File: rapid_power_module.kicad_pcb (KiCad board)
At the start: 4 copper layers, 80 x 136 mm, 198 parts, among them J1 Conn_02x04_Top_Bottom, J11 SWD Header, J12 SWD Header, J16 USB_C_Receptacle_USB2.0, J17 TC2050, J2 Conn_02x03_Odd_Even, J3 Conn_02x04_Top_Bottom, J4 Conn_02x03_Odd_Even, J5 Molex MicroFit 2x2, J6 Molex MicroFit 2x2, J7 Molex MicroFit 2x2, J8 Molex MicroFit 2x2, J9 Molex MicroFit 2x2, Q1 Q_PMOS, Q2 Q_PMOS, Q3 Q_PMOS, Q4 Q_PMOS, Q5 NMOS, Q6 NMOS, Q7 NMOS, Q8 NMOS, SW1 KMR721NGLFS, SW2 KMR721NGLFS, U1 BQ25756RRVR, U10 L7805, U11 MCP2562-E-SN, U12 STM32F105RCTx, U13 AZ1117I-3.3, U14 TPD4E1U06, U15 TPD4E1U06, U2 CYPD3177-24LQ, U3 BQ76952PFBR, Y3 8MHz 12pF

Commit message: Further Routing work and fixed the Q Pins
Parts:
- removed Q4: Q_PMOS, Package_SO:Diodes_SO-8EP
- added Q12: AOSP21321, Package_SO:SO-8_3.9x4.9mm_P1.27mm, F.Cu at (203.9, 63.6)
- Q1, Q2, Q3: value Q_PMOS -> AOSP21321; footprint Package_SO:Diodes_SO-8EP -> Package_SO:SO-8_3.9x4.9mm_P1.27mm
- Q5, Q6, Q7, Q8: moved to F.Cu
- moved Q8 58.8 mm to (127.0, 37.2), turned to 0 degrees
- moved Q7 58.0 mm to (127.0, 43.2), turned to 0 degrees
- moved Q5 24.2 mm to (143.9, 43.3)
- moved Q6 12.6 mm to (143.9, 37.3)
- moved D24 10.8 mm to (152.5, 33.5)
- moved C12 9.68 mm to (161.8, 40.7)
- moved C13 9.68 mm to (160.8, 40.7)
- moved C9 9.68 mm to (157.1, 39.1)
- moved R18 9.68 mm to (165.8, 41.3)
- moved R5 9.68 mm to (165.6, 37.1)
- moved C10 9.68 mm to (160.5, 33.0)
- moved C11 9.68 mm to (159.7, 40.7)
- moved R10 9.68 mm to (162.7, 40.7)
- moved R13 9.68 mm to (165.5, 35.0)
- moved R19 9.68 mm to (165.7, 40.2)
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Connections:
- C10 pad 2: Net-(C10-Pad2) -> Net-(Q1-G)
- C9 pad 2: Net-(C10-Pad2) -> Net-(Q1-G)
- Q1 pad 1: (no net) -> USB_PD_OUT
- Q1 pad 2: (no net) -> USB_PD_OUT
- Q1 pad 3: (no net) -> USB_PD_OUT
- Q1 pad 4: (no net) -> Net-(Q1-G)
- Q1 pad 5: (no net) -> Net-(Q1-D-Pad5)
- Q1 pad 6: (no net) -> Net-(Q1-D-Pad5)
- Q1 pad 7: (no net) -> Net-(Q1-D-Pad5)
- Q1 pad 8: (no net) -> Net-(Q1-D-Pad5)
- Q2 pad 1: (no net) -> Net-(Q2-S-Pad1)
- Q2 pad 2: (no net) -> Net-(Q2-S-Pad1)
- Q2 pad 3: (no net) -> Net-(Q2-S-Pad1)
- Q2 pad 4: (no net) -> Net-(Q2-G)
- Q2 pad 5: (no net) -> /VBUS
- Q2 pad 6: (no net) -> /VBUS
- Q2 pad 7: (no net) -> /VBUS
- Q2 pad 8: (no net) -> /VBUS
- Q3 pad 1: (no net) -> SAFE_PWR_OUT
- Q3 pad 2: (no net) -> SAFE_PWR_OUT
- Q3 pad 3: (no net) -> SAFE_PWR_OUT
- Q3 pad 4: (no net) -> Net-(Q2-G)
- Q3 pad 5: (no net) -> Net-(Q2-S-Pad1)
- Q3 pad 6: (no net) -> Net-(Q2-S-Pad1)
- Q3 pad 7: (no net) -> Net-(Q2-S-Pad1)
- Q3 pad 8: (no net) -> Net-(Q2-S-Pad1)
- Q5 pad 4: (no net) -> unconnected-(Q5-G-Pad4)
- Q5 pad 5: (no net) -> unconnected-(Q5-D-Pad5)
- R4 pad 2: Net-(C10-Pad2) -> Net-(Q1-G)
- R5 pad 1: Net-(C10-Pad2) -> Net-(Q1-G)
- R8 pad 2: Net-(Q3-PadG) -> Net-(Q2-G)
- R9 pad 1: Net-(Q3-PadG) -> Net-(Q2-G)

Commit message: Further Routing work and fixed the Q Pins
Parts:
- removed Q8: NMOS, Package_SON:Infineon_PG-TDSON-8_6.15x5.15mm
- added Q4: HiDRV1, Package_TO_SOT_SMD:TDSON-8-1, F.Cu at (127.0, 37.0)
- added R25: 20k, Resistor_SMD:R_0402_1005Metric, F.Cu at (191.5, 46.5)
- added R27: 50k, Resistor_SMD:R_0402_1005Metric, F.Cu at (191.5, 48.5)
- Q5: value NMOS -> LoDRV1; footprint Package_SON:Infineon_PG-TDSON-8_6.15x5.15mm -> Package_TO_SOT_SMD:TDSON-8-1
- Q6: value NMOS -> HiDRV2; footprint Package_SON:Infineon_PG-TDSON-8_6.15x5.15mm -> Package_TO_SOT_SMD:TDSON-8-1
- Q7: value NMOS -> LoDRV2; footprint Package_SON:Infineon_PG-TDSON-8_6.15x5.15mm -> Package_TO_SOT_SMD:TDSON-8-1
- R83, R97: footprint Resistor_SMD:R_0603_1608Metric -> Resistor_SMD:R_0402_1005Metric
- R94: value 16k -> 20k; footprint Resistor_SMD:R_0603_1608Metric -> Resistor_SMD:R_0402_1005Metric
- R95: value 8k -> 10k; footprint Resistor_SMD:R_0603_1608Metric -> Resistor_SMD:R_0402_1005Metric
- R96: value 4k -> 5.1k; footprint Resistor_SMD:R_0603_1608Metric -> Resistor_SMD:R_0402_1005Metric
- R98: value 12.5k -> 15k
- moved C49 46.8 mm to (119.5, 42.0)
- moved Q7 17.0 mm to (144.0, 43.0), turned to 180 degrees
- moved Q5 16.9 mm to (127.0, 43.0), turned to 0 degrees
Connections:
- BT1 pad N: (no net) -> Net-(BT1--)
- BT1 pad P: (no net) -> PACK+
- BT2 pad N: (no net) -> Net-(BT2--)
- BT2 pad P: (no net) -> Net-(BT1--)
- BT3 pad N: (no net) -> PACK-
- BT3 pad P: (no net) -> Net-(BT2--)
- C1 pad 2: ISNK_FINE -> PACK-
- C11 pad 2: ISNK_FINE -> PACK-
- C12 pad 2: ISNK_FINE -> PACK-
- C13 pad 2: ISNK_FINE -> PACK-
- C16 pad 2: ISNK_FINE -> PACK-
- C17 pad 1: ISNK_FINE -> PACK-
- C19 pad 1: ISNK_FINE -> PACK-
- C2 pad 2: ISNK_FINE -> PACK-
- C21 pad 1: ISNK_FINE -> PACK-
- C24 pad 1: ISNK_FINE -> PACK-
- C3 pad 2: ISNK_FINE -> PACK-
- C37 pad 1: ISNK_FINE -> PACK-
- C38 pad 2: ISNK_FINE -> PACK-
- C4 pad 1: Net-(C4-Pad1) -> Net-(Q4-D)
- C4 pad 2: ISNK_FINE -> PACK-
- C44 pad 2: ISNK_FINE -> PACK-
- C45 pad 1: ISNK_FINE -> PACK-
- C47 pad 2: ISNK_FINE -> PACK-
- C48 pad 2: ISNK_FINE -> PACK-
- C5 pad 2: ISNK_FINE -> PACK-
- C58 pad 1: ISNK_FINE -> PACK-
- C59 pad 1: ISNK_FINE -> PACK-
- C6 pad 2: ISNK_FINE -> PACK-
- C60 pad 2: ISNK_FINE -> PACK-
- C61 pad 1: ISNK_FINE -> PACK-
- C62 pad 2: ISNK_FINE -> PACK-
- C65 pad 2: ISNK_FINE -> PACK-
- C67 pad 2: ISNK_FINE -> PACK-
- C68 pad 2: ISNK_FINE -> PACK-
- C69 pad 2: ISNK_FINE -> PACK-
- C7 pad 1: Net-(C4-Pad1) -> Net-(Q4-D)
- C7 pad 2: ISNK_FINE -> PACK-
- C70 pad 2: ISNK_FINE -> PACK-
- C71 pad 2: ISNK_FINE -> PACK-
- C72 pad 2: ISNK_FINE -> PACK-
- C73 pad 2: ISNK_FINE -> PACK-
- C74 pad 2: ISNK_FINE -> PACK-
- C75 pad 2: ISNK_FINE -> PACK-
- C76 pad 2: ISNK_FINE -> PACK-
- C77 pad 2: ISNK_FINE -> PACK-
- C78 pad 2: ISNK_FINE -> PACK-
- C79 pad 1: ISNK_FINE -> PACK-
- C8 pad 2: ISNK_FINE -> PACK-
- C80 pad 1: ISNK_FINE -> PACK-
- C81 pad 2: ISNK_FINE -> PACK-
- C82 pad 2: ISNK_FINE -> PACK-
- C83 pad 2: ISNK_FINE -> PACK-
- C84 pad 2: ISNK_FINE -> PACK-
- C85 pad 2: ISNK_FINE -> PACK-
- C86 pad 2: ISNK_FINE -> PACK-
- C87 pad 2: ISNK_FINE -> PACK-
- C88 pad 2: ISNK_FINE -> PACK-
- C89 pad 2: ISNK_FINE -> PACK-
- C90 pad 2: ISNK_FINE -> PACK-
- C91 pad 2: ISNK_FINE -> PACK-
- D20 pad 1: ISNK_FINE -> PACK-
- D21 pad 1: ISNK_FINE -> PACK-
- D24 pad 2: ISNK_FINE -> PACK-
- H1 pad 1: ISNK_FINE -> PACK-
- H2 pad 1: ISNK_FINE -> PACK-
- H3 pad 1: ISNK_FINE -> PACK-
- H4 pad 1: ISNK_FINE -> PACK-
- J1 pad 1: ISNK_FINE -> PACK-
- J1 pad 2: ISNK_FINE -> PACK-
- J11 pad 4: ISNK_FINE -> PACK-
- J12 pad 4: ISNK_FINE -> PACK-
- J16 pad A1: ISNK_FINE -> PACK-
- J16 pad A12: ISNK_FINE -> PACK-
- J16 pad B1: ISNK_FINE -> PACK-
- J16 pad B12: ISNK_FINE -> PACK-
- J16 pad S1: ISNK_FINE -> PACK-
- J17 pad 3: ISNK_FINE -> PACK-
- J17 pad 4: ISNK_FINE -> PACK-
- J2 pad 1: unconnected-(J2-Pin_1-Pad1) -> Net-(J2-Pin_1)
- J3 pad 1: ISNK_FINE -> PACK-
- J3 pad 2: ISNK_FINE -> PACK-
- J4 pad 1: unconnected-(J4-Pin_1-Pad1) -> Net-(J4-Pin_1)
- J6 pad 1: ISNK_FINE -> PACK-
- J6 pad 2: ISNK_FINE -> PACK-
- J7 pad 1: ISNK_FINE -> PACK-
- J7 pad 2: ISNK_FINE -> PACK-
- J8 pad 1: ISNK_FINE -> PACK-
- J8 pad 2: ISNK_FINE -> PACK-
- J9 pad 1: ISNK_FINE -> PACK-
- J9 pad 2: ISNK_FINE -> PACK-
- Q5 pad 1: Net-(C4-Pad1) -> PACK-
- Q5 pad 2: HIDRV1 -> PACK-
- Q5 pad 3: SW1 -> PACK-
- Q5 pad 4: unconnected-(Q5-G-Pad4) -> LODRV1
- Q5 pad 5: unconnected-(Q5-D-Pad5) -> SW1
- Q6 pad 1: SW1 -> SW2
- Q6 pad 2: LODRV1 -> SW2
- Q6 pad 3: ISNK_FINE -> SW2
- Q6 pad 4: (no net) -> HIDRV2
- Q6 pad 5: (no net) -> BuckBoostOut
- Q7 pad 1: SW2 -> PACK-
- Q7 pad 2: LODRV2 -> PACK-
- Q7 pad 3: ISNK_FINE -> PACK-
- Q7 pad 4: (no net) -> LODRV2
- Q7 pad 5: (no net) -> SW2
- R13 pad 2: ISNK_FINE -> PACK-
- R19 pad 2: ISNK_FINE -> PACK-
- R20 pad 1: ISNK_FINE -> PACK-
- R23 pad 2: ISNK_FINE -> PACK-
- R24 pad 2: ISNK_FINE -> PACK-
- R31 pad 2: ISNK_FINE -> PACK-
- R43 pad 2: ISNK_FINE -> PACK-
- R65 pad 2: Net-(C4-Pad1) -> Net-(Q4-D)
- R7 pad 2: ISNK_FINE -> PACK-
- R76 pad 1: ISNK_FINE -> PACK-
- R79 pad 1: Net-(C4-Pad1) -> Net-(Q4-D)
- R82 pad 2: ISNK_FINE -> PACK-
- R83 pad 2: ISNK_FINE -> PACK-
- R91 pad 1: ISNK_FINE -> PACK-
- R94 pad 2: ISNK_FINE -> PACK-
- R95 pad 2: ISNK_FINE -> PACK-
- R96 pad 2: ISNK_FINE -> PACK-
- R97 pad 2: ISNK_FINE -> PACK-
- R98 pad 2: ISNK_FINE -> PACK-
- SW2 pad 1: ISNK_FINE -> PACK-
- TH1 pad 2: ISNK_FINE -> PACK-
- U1 pad 17: ISNK_FINE -> PACK-
- U1 pad 22: ISNK_FINE -> PACK-
- U1 pad 37: ISNK_FINE -> PACK-
- U10 pad 2: ISNK_FINE -> PACK-
- U11 pad 2: ISNK_FINE -> PACK-
- U11 pad 8: ISNK_FINE -> PACK-
- U12 pad 12: ISNK_FINE -> PACK-
- U12 pad 18: ISNK_FINE -> PACK-
- U12 pad 31: ISNK_FINE -> PACK-
- U12 pad 47: ISNK_FINE -> PACK-
- U12 pad 63: ISNK_FINE -> PACK-
- U13 pad 1: ISNK_FINE -> PACK-
- U14 pad 3: ISNK_FINE -> PACK-
- U15 pad 3: ISNK_FINE -> PACK-
- U2 pad 19: ISNK_FINE -> PACK-
- U2 pad 22: ISNK_FINE -> PACK-
- U2 pad 25: ISNK_FINE -> PACK-
- U2 pad 6: ISNK_FINE -> PACK-
- U3 pad 17: ISNK_FINE -> PACK-
- U3 pad 18: ISNK_FINE -> PACK-
- U3 pad 20: ISNK_FINE -> PACK-
- U3 pad 41: ISNK_FINE -> PACK-
- Y3 pad 2: ISNK_FINE -> PACK-
- Y3 pad 4: ISNK_FINE -> PACK-
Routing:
- net PACK-: track 0.00 -> 16.6 mm, vias 0 -> 1
- net ISNK_FINE: track 13.3 -> 0.00 mm
- net (no net): track 145.4 -> 142.1 mm, vias 1 -> 0

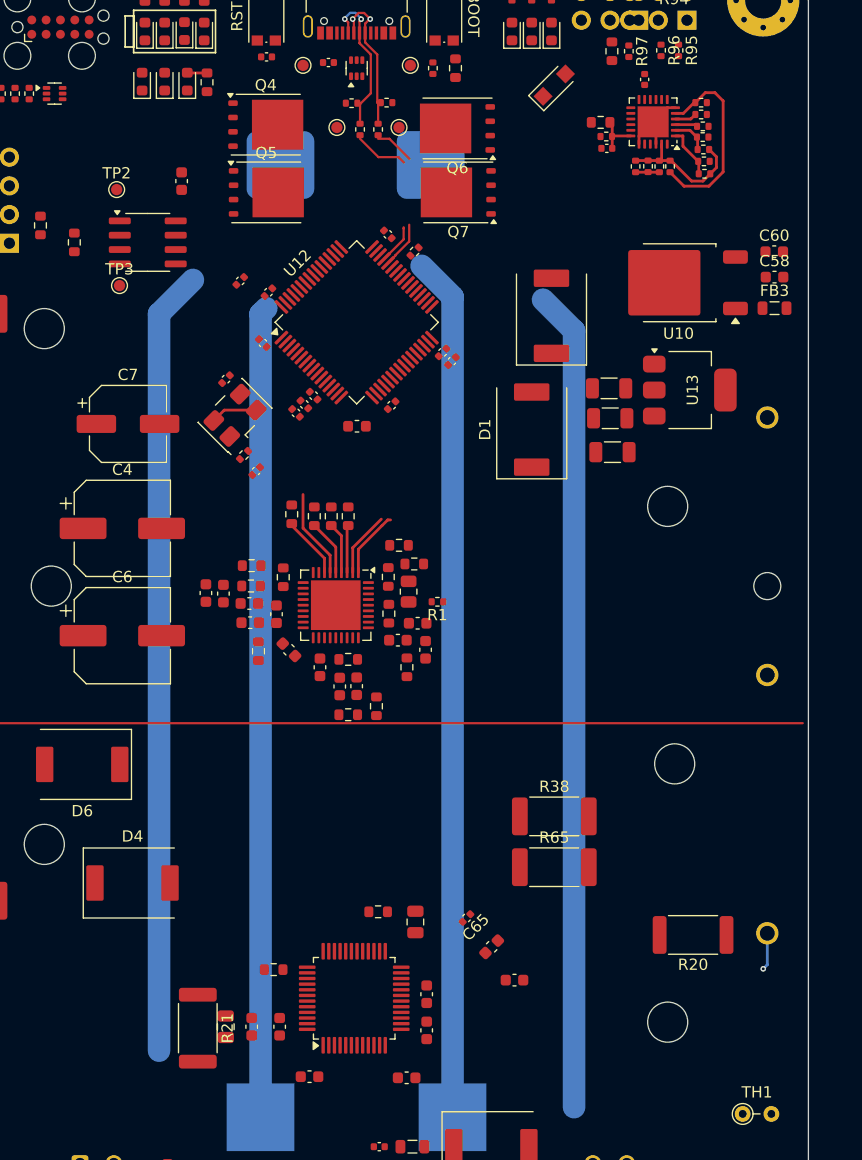
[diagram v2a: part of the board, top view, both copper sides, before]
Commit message: Placed the  NMOS near Inductor, moved STM out of the way and fixed the Battery Pins
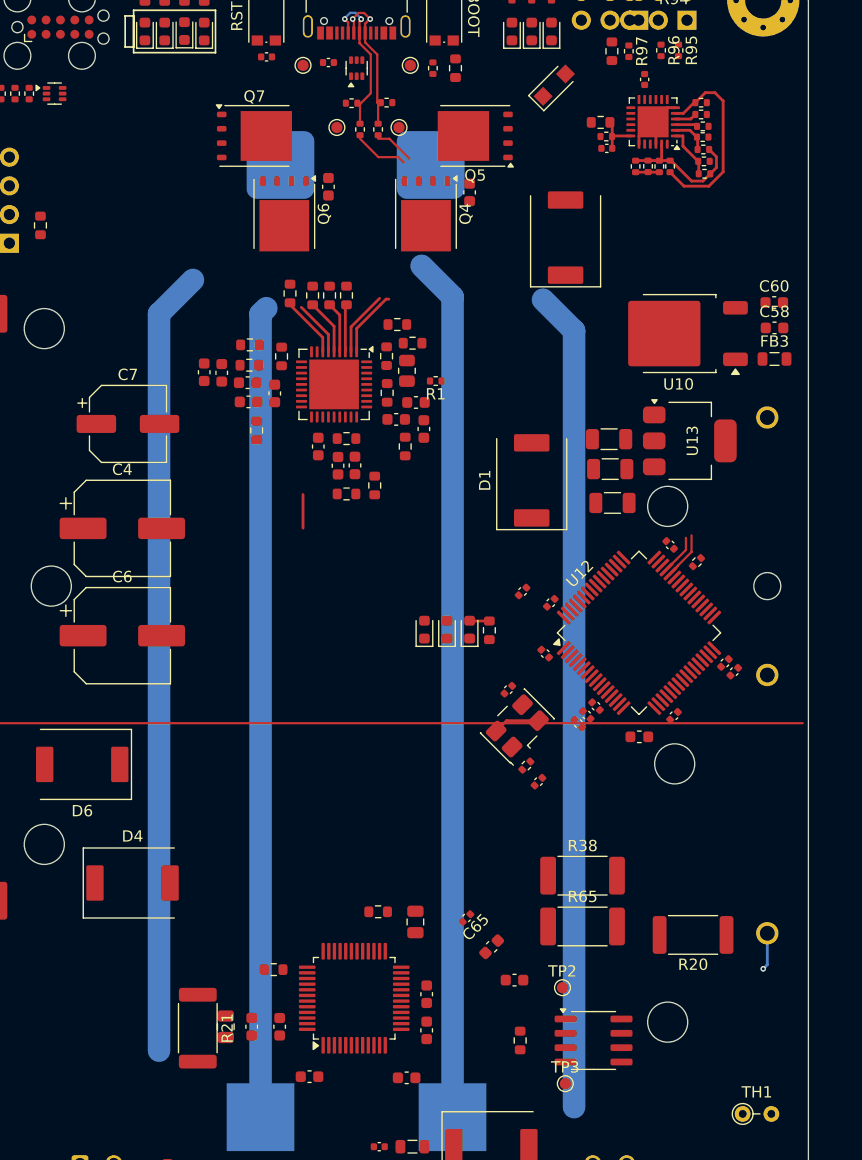
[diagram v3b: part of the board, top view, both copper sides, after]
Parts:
- moved R35 80.9 mm to (149.5, 118.1)
- moved TP2 80.9 mm to (153.2, 113.4)
- moved TP3 80.9 mm to (153.5, 121.9)
- moved U11 80.9 mm to (156.0, 118.1)
- moved D20 54.6 mm to (141.0, 81.7)
- moved D21 54.6 mm to (143.0, 81.7)
- moved D22 54.6 mm to (145.0, 81.7)
- moved R69 54.6 mm to (146.8, 81.8)
- moved C46 41.1 mm to (132.5, 42.5), turned to -90 degrees
- moved C73 37.2 mm to (156.2, 88.5)
- moved C77 37.2 mm to (151.1, 95.2)
- moved R74 37.2 mm to (150.0, 93.8)
- moved Y3 37.2 mm to (149.2, 90.2)
- moved C70 37.2 mm to (162.8, 74.2)
- moved C71 37.2 mm to (167.6, 84.7)
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
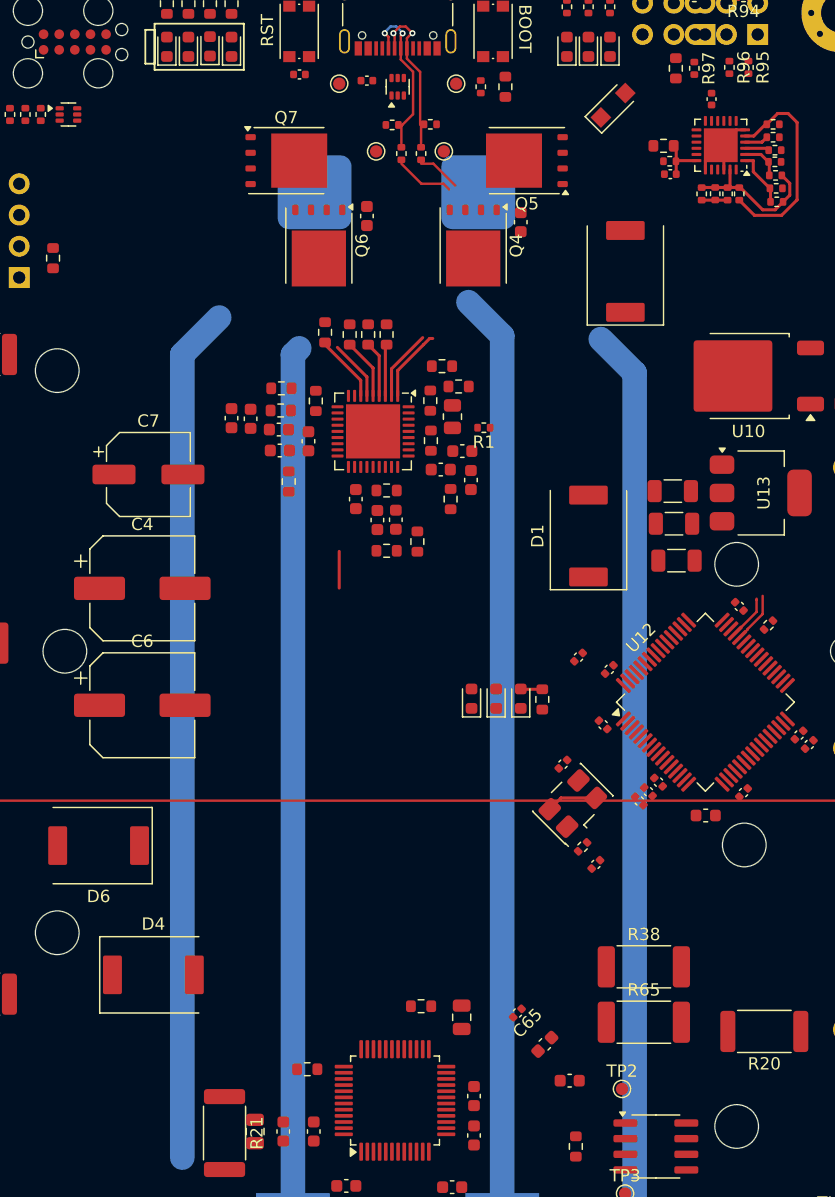
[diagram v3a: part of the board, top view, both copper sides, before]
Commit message: Fixed wuerth cap footprints and values
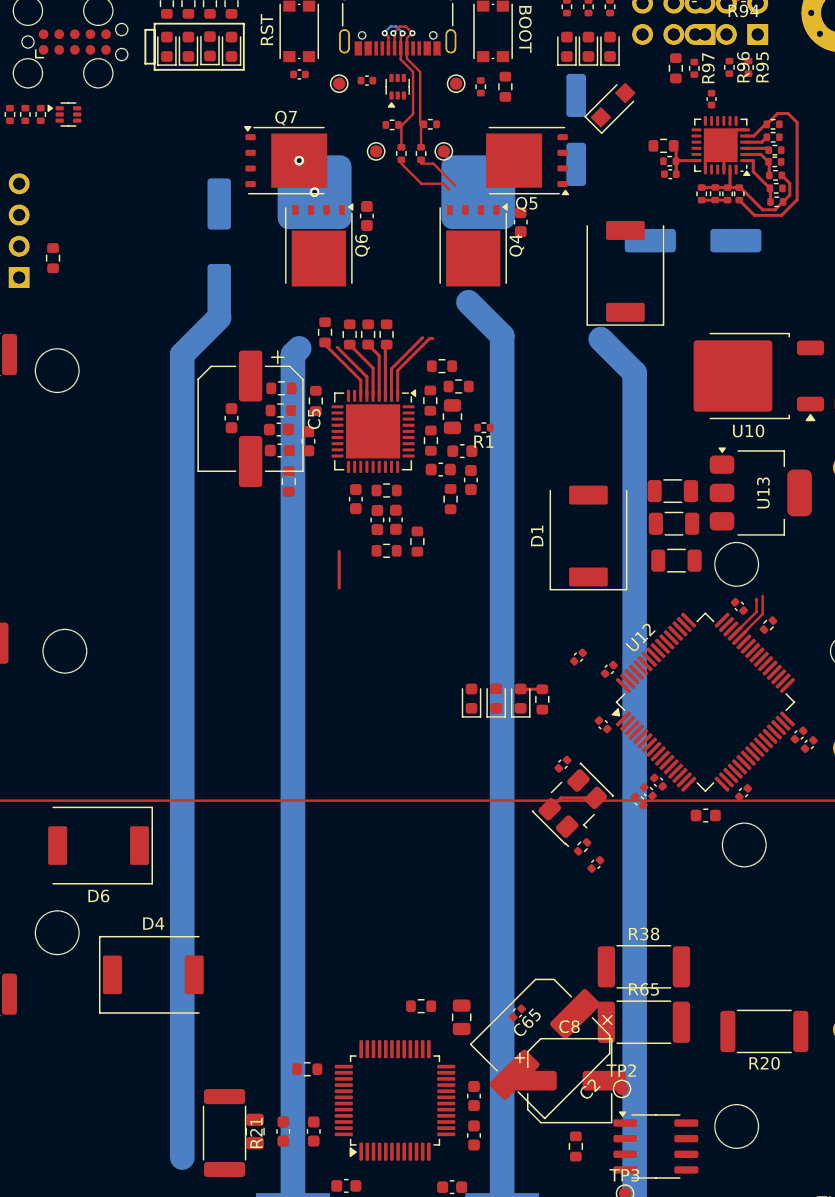
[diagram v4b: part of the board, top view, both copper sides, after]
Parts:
- C2, C5: footprint Capacitor_SMD:C_0603_1608Metric -> Capacitor_SMD:CP_Elec_8x6.9
- C4, C6: value 174u -> 82u; moved to B.Cu
- C7: moved to B.Cu
- C8: footprint Capacitor_SMD:C_0603_1608Metric -> Capacitor_SMD:CP_Elec_6.3x5.9
- moved C4 52.9 mm to (159.0, 44.5)
- moved C7 44.6 mm to (149.5, 35.5), turned to 90 degrees
- moved C6 37.8 mm to (120.5, 45.0), turned to -90 degrees
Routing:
- net PACK-: track 16.6 -> 86.1 mm
- net (no net): track 142.1 -> 72.6 mm
- net SW2: vias 0 -> 2
